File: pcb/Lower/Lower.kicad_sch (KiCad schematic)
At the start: 34 parts

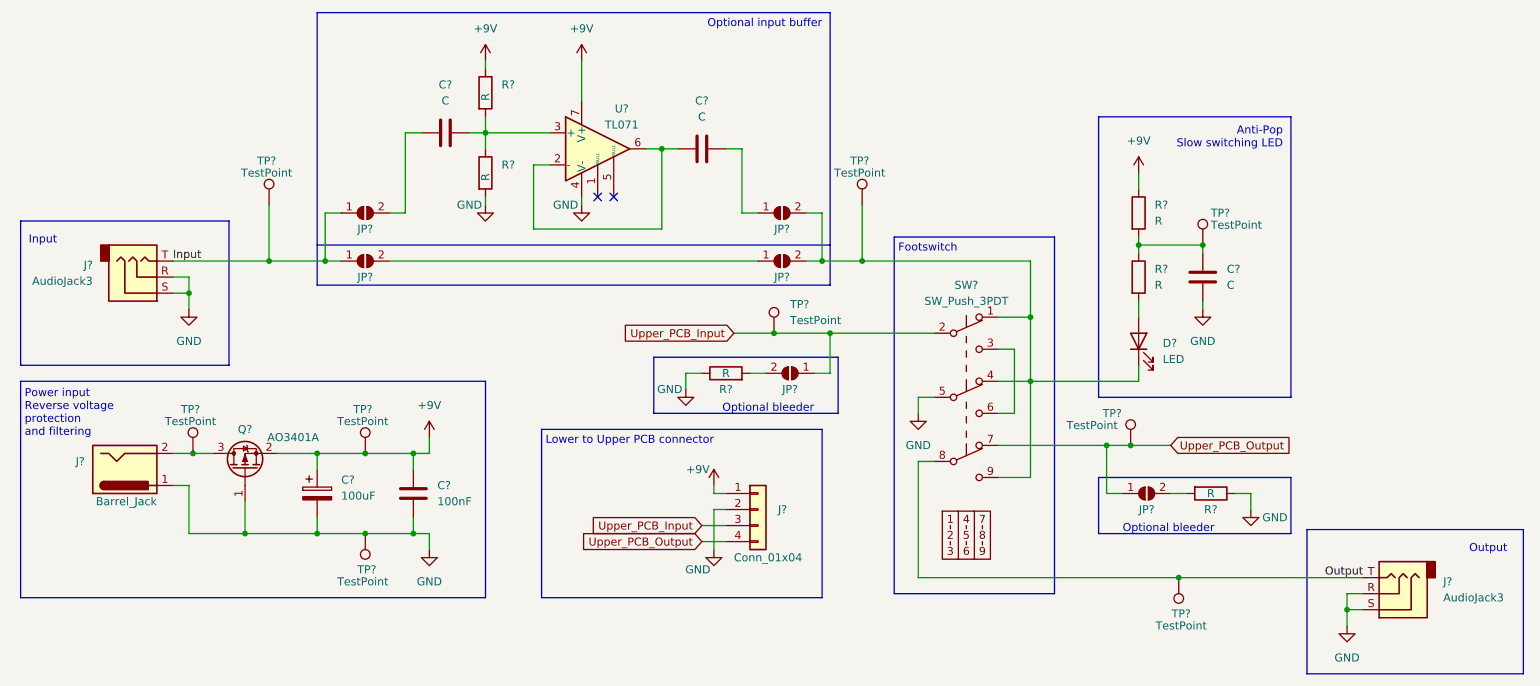
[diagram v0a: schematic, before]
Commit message: Assign Lower PCB footprints and BOM codes
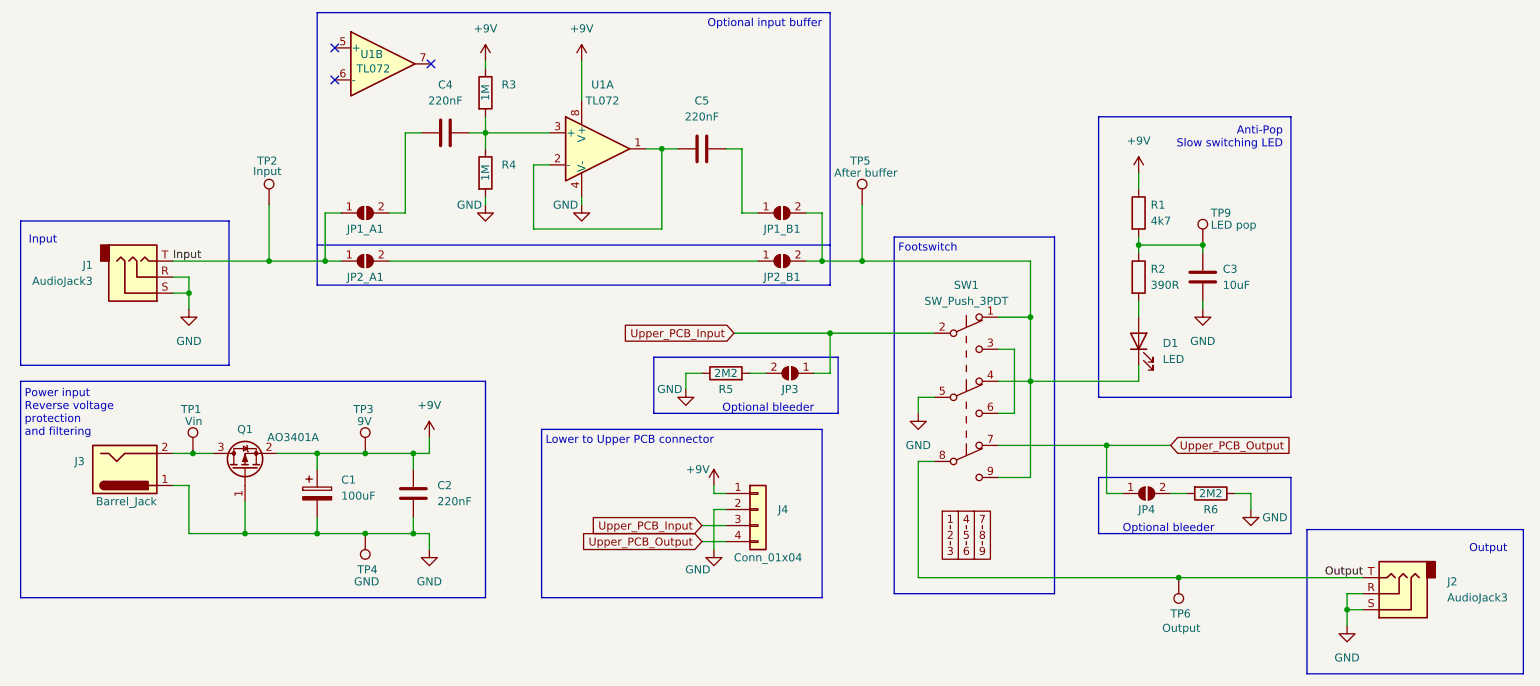
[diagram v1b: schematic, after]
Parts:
- removed C?: 100nF, symbol Device:C
- removed TP? (x2): TestPoint, symbol Connector:TestPoint
- removed U?: TL071, symbol Amplifier_Operational:TL071
- added C2: 220nF, Capacitor_SMD:C_0603_1608Metric, symbol Device:C
- added U1: TL072, Package_SO:SOIC-8_3.9x4.9mm_P1.27mm, symbol Amplifier_Operational:TL072
- C1: renamed from C?; footprint (none) -> Capacitor_SMD:CP_Elec_6.3x5.8; LCSC (none) -> C249982
- C3: renamed from C?; value C -> 10uF; footprint (none) -> Capacitor_SMD:C_0805_2012Metric; LCSC (none) -> C15850
- C4, C5: renamed from C?; value C -> 220nF; footprint (none) -> Capacitor_SMD:C_0603_1608Metric; LCSC (none) -> C21120
- D1: renamed from D?; footprint (none) -> LED_THT:LED_D5.0mm; LCSC (none) -> C417347
- J4: renamed from J?; footprint (none) -> Connector_PinSocket_2.54mm:PinSocket_1x04_P2.54mm_Vertical; now left out of the parts list
- JP1_A1, JP1_B1, JP2_A1, JP2_B1, JP3, JP4: renamed from JP?; footprint (none) -> Jumper:SolderJumper-2_P1.3mm_Open_TrianglePad1.0x1.5mm; now left out of the parts list
- Q1: renamed from Q?; LCSC (none) -> C15127
- R1: renamed from R?; value R -> 4k7; footprint (none) -> Resistor_SMD:R_0603_1608Metric
- R2: renamed from R?; value R -> 390R; footprint (none) -> Resistor_SMD:R_0603_1608Metric
- R3, R4: renamed from R?; value R -> 1M; footprint (none) -> Resistor_SMD:R_0603_1608Metric
- R5, R6: renamed from R?; value R -> 2M2; footprint (none) -> Resistor_SMD:R_0603_1608Metric
- SW1: renamed from SW?; footprint (none) -> MeineBib:Footswitch_3PDT
- TP1: renamed from TP?; value TestPoint -> Vin; footprint (none) -> TestPoint:TestPoint_Pad_D2.0mm; now left out of the parts list
- TP2: renamed from TP?; value TestPoint -> Input; footprint (none) -> TestPoint:TestPoint_Bridge_Pitch2.54mm_Drill1.0mm; now left out of the parts list
- TP3: renamed from TP?; value TestPoint -> 9V; footprint (none) -> TestPoint:TestPoint_Pad_D2.0mm; now left out of the parts list
- TP4: renamed from TP?; value TestPoint -> GND; footprint (none) -> TestPoint:TestPoint_Bridge_Pitch2.54mm_Drill1.0mm; now left out of the parts list
- TP5: renamed from TP?; value TestPoint -> After buffer; footprint (none) -> TestPoint:TestPoint_Pad_D2.0mm; now left out of the parts list
- TP6: renamed from TP?; value TestPoint -> Output; footprint (none) -> TestPoint:TestPoint_Bridge_Pitch2.54mm_Drill1.0mm; now left out of the parts list
- TP9: renamed from TP?; value TestPoint -> LED pop; footprint (none) -> TestPoint:TestPoint_Pad_D2.0mm; now left out of the parts list
- gave numbers to parts that had none: 3
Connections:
- net +9V: now also C2.1, U1.8 (V+)
- net GND: now also C2.2, U1.4 (V-)
- net at C4.2, R3.2, R4.1: now also U1.3 (+)
- net at C5.1: now also U1.1, U1.2 (-)
- no-connect marks 2 -> 3

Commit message: [Lower] Design and add more footprints
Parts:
- J1, J2: footprint (none) -> MeineBib:Audio_Jack_PJ-602B
- J3: footprint (none) -> MeineBib:DC_Barrel_Jack_Thinline_Wired_Standing
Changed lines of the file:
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@@
       (effects (font (size 1.27 1.27)) (justify right))
     )
-    (property "Footprint" "" (id 2) (at 52.07 92.71 0)
+    (property "Footprint" "MeineBib:Audio_Jack_PJ-602B" (id 2) (at 52.07 92.71 0)
       (effects (font (size 1.27 1.27)) hide)
     )
@@
       (effects (font (size 1.27 1.27)) (justify right))
     )
-    (property "Footprint" "" (id 2) (at 50.8 122.174 0)
+    (property "Footprint" "MeineBib:DC_Barrel_Jack_Thinline_Wired_Standing" (id 2) (at 50.8 122.174 0)
       (effects (font (size 1.27 1.27)) hide)
     )
@@
       (effects (font (size 1.27 1.27)) (justify right))
     )
-    (property "Footprint" "" (id 2) (at 250.825 142.875 0)
+    (property "Footprint" "MeineBib:Audio_Jack_PJ-602B" (id 2) (at 250.825 142.875 0)
       (effects (font (size 1.27 1.27)) hide)
     )
@@
     )
     (path "/37778a1f-86de-4449-abb1-14af5009805a"
-      (reference "J1") (unit 1) (value "AudioJack3") (footprint "")
+      (reference "J1") (unit 1) (value "AudioJack3") (footprint "MeineBib:Audio_Jack_PJ-602B")
     )
     (path "/ce833355-b6f2-4a51-9de8-dda19b75db2a"
-      (reference "J2") (unit 1) (value "AudioJack3") (footprint "")
+      (reference "J2") (unit 1) (value "AudioJack3") (footprint "MeineBib:Audio_Jack_PJ-602B")
     )
     (path "/680b3e96-c480-445f-a2bf-28a5c2056d8e"
-      (reference "J3") (unit 1) (value "Barrel_Jack") (footprint "")
+      (reference "J3") (unit 1) (value "Barrel_Jack") (footprint "MeineBib:DC_Barrel_Jack_Thinline_Wired_Standing")
     )
     (path "/43624bd7-5b28-4455-bedf-a59e39f0128d"

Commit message: [Lower] Update Anti-Pop circuit after testing
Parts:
- R2: renamed from R1; value 4k7 -> 2k2
- renumbered R2 to R1
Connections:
- net +9V: now also R1.1; no longer R2.1
- net at D1.2 (A): now also R2.2; no longer R1.2
- net at C3.1, TP9.1: now also R1.2, R2.1; no longer R1.1, R2.2
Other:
- moved on the sheet: R1, R2
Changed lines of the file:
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@@
     (pin "2")
   )
-  (symbol (lib_id "Device:R") (at 210.185 82.55 0) (unit 1)
-    (in_bom yes) (on_board yes) (fields_autoplaced)
-    (property "Reference" "R1" (id 0) (at 212.09 81.2799 0)
-      (effects (font (size 1.27 1.27)) (justify left))
-    )
-    (property "Value" "4k7" (id 1) (at 212.09 83.8199 0)
-      (effects (font (size 1.27 1.27)) (justify left))
-    )
-    (property "Footprint" "Resistor_SMD:R_0603_1608Metric" (id 2) (at 208.407 82.55 90)
-      (effects (font (size 1.27 1.27)) hide)
-    )
-    (property "Datasheet" "~" (id 3) (at 210.185 82.55 0)
+  (symbol (lib_id "Device:R") (at 210.185 92.71 0) (unit 1)
+    (in_bom yes) (on_board yes) (fields_autoplaced)
+    (property "Reference" "R2" (id 0) (at 212.09 91.4399 0)
+      (effects (font (size 1.27 1.27)) (justify left))
+    )
+    (property "Value" "2k2" (id 1) (at 212.09 93.9799 0)
+      (effects (font (size 1.27 1.27)) (justify left))
+    )
+    (property "Footprint" "Resistor_SMD:R_0603_1608Metric" (id 2) (at 208.407 92.71 90)
+      (effects (font (size 1.27 1.27)) hide)
+    )
+    (property "Datasheet" "~" (id 3) (at 210.185 92.71 0)
       (effects (font (size 1.27 1.27)) hide)
     )
@@
     (pin "1")
   )
-  (symbol (lib_id "Device:R") (at 210.185 92.71 0) (unit 1)
-    (in_bom yes) (on_board yes) (fields_autoplaced)
-    (property "Reference" "R2" (id 0) (at 212.09 91.4399 0)
-      (effects (font (size 1.27 1.27)) (justify left))
-    )
-    (property "Value" "390R" (id 1) (at 212.09 93.9799 0)
-      (effects (font (size 1.27 1.27)) (justify left))
-    )
-    (property "Footprint" "Resistor_SMD:R_0603_1608Metric" (id 2) (at 208.407 92.71 90)
-      (effects (font (size 1.27 1.27)) hide)
-    )
-    (property "Datasheet" "~" (id 3) (at 210.185 92.71 0)
+  (symbol (lib_id "Device:R") (at 210.185 82.55 0) (unit 1)
+    (in_bom yes) (on_board yes)
+    (property "Reference" "R1" (id 0) (at 212.09 81.2799 0)
+      (effects (font (size 1.27 1.27)) (justify left))
+    )
+    (property "Value" "390R" (id 1) (at 212.09 83.82 0)
+      (effects (font (size 1.27 1.27)) (justify left))
+    )
+    (property "Footprint" "Resistor_SMD:R_0603_1608Metric" (id 2) (at 208.407 82.55 90)
+      (effects (font (size 1.27 1.27)) hide)
+    )
+    (property "Datasheet" "~" (id 3) (at 210.185 82.55 0)
       (effects (font (size 1.27 1.27)) hide)
     )
@@
       (reference "Q1") (unit 1) (value "AO3401A") (footprint "Package_TO_SOT_SMD:SOT-23")
     )
+    (path "/c5dde4d4-1f05-4ce8-a9a0-135e7142ecd2"
+      (reference "R1") (unit 1) (value "390R") (footprint "Resistor_SMD:R_0603_1608Metric")
+    )
     (path "/0ec435e0-2219-4036-8fc8-9d64c1b535ad"
-      (reference "R1") (unit 1) (value "4k7") (footprint "Resistor_SMD:R_0603_1608Metric")
-    )
-    (path "/c5dde4d4-1f05-4ce8-a9a0-135e7142ecd2"
-      (reference "R2") (unit 1) (value "390R") (footprint "Resistor_SMD:R_0603_1608Metric")
+      (reference "R2") (unit 1) (value "2k2") (footprint "Resistor_SMD:R_0603_1608Metric")
     )
     (path "/6685e374-4b74-4363-b25d-dd27bd2656c7"

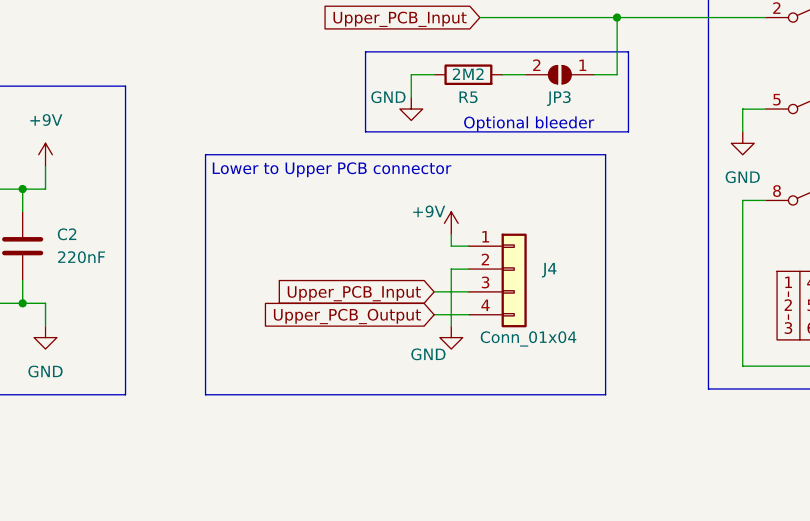
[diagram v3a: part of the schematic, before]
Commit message: [Lower] Pinswap PCB-PCB connector
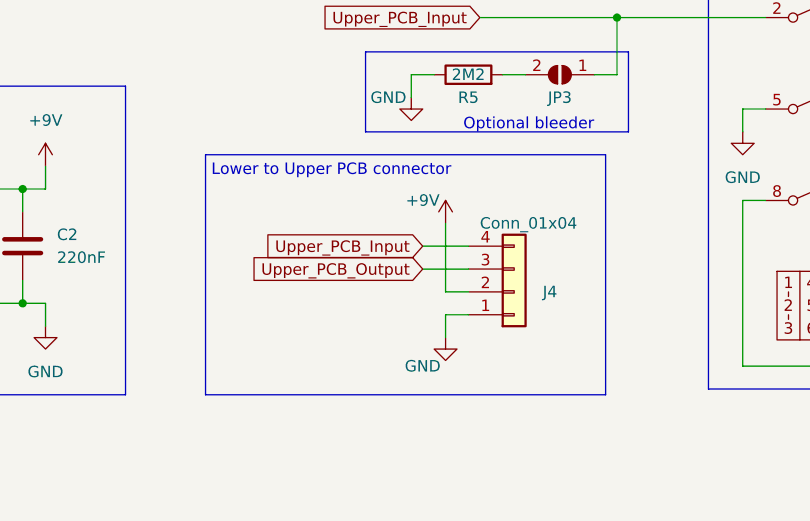
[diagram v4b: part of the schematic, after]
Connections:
- net +9V: now also J4.2 (Pin_2); no longer J4.1 (Pin_1)
- net GND: now also J4.1 (Pin_1); no longer J4.2 (Pin_2)
- net Upper_PCB_Input: now also J4.4 (Pin_4); no longer J4.3 (Pin_3)
- net Upper_PCB_Output: now also J4.3 (Pin_3); no longer J4.4 (Pin_4)
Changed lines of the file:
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@@
+    (stroke (width 0) (type default) (color 0 0 0 0))
+  )
+  (wire (pts (xy 144.78 134.62) (xy 142.24 134.62))
     (stroke (width 0) (type default) (color 0 0 0 0))
   )
@@
     (stroke (width 0) (type default) (color 0 0 0 0))
   )
+  (wire (pts (xy 142.24 124.46) (xy 142.24 132.08))
+    (stroke (width 0) (type default) (color 0 0 0 0))
+  )
   (wire (pts (xy 104.14 69.85) (xy 106.68 69.85))
     (stroke (width 0) (type default) (color 0 0 0 0))
@@
     (stroke (width 0) (type default) (color 0 0 0 0))
   )
-  (wire (pts (xy 140.97 134.62) (xy 144.78 134.62))
-    (stroke (width 0) (type default) (color 0 0 0 0))
-  )
   (polyline (pts (xy 66.04 106.68) (xy 66.04 83.82))
     (stroke (width 0) (type default) (color 0 0 0 0))
@@
     (stroke (width 0) (type default) (color 0 0 0 0))
   )
-  (wire (pts (xy 144.78 129.54) (xy 142.875 129.54))
-    (stroke (width 0) (type default) (color 0 0 0 0))
-  )
   (wire (pts (xy 80.01 130.81) (xy 80.01 133.35))
     (stroke (width 0) (type default) (color 0 0 0 0))
@@
     (stroke (width 0) (type default) (color 0 0 0 0))
   )
-  (wire (pts (xy 140.97 132.08) (xy 144.78 132.08))
-    (stroke (width 0) (type default) (color 0 0 0 0))
-  )
   (polyline (pts (xy 33.02 109.22) (xy 106.68 109.22))
     (stroke (width 0) (type default) (color 0 0 0 0))
@@
     (stroke (width 0) (type default) (color 0 0 0 0))
   )
+  (wire (pts (xy 139.7 129.54) (xy 144.78 129.54))
+    (stroke (width 0) (type default) (color 0 0 0 0))
+  )
   (wire (pts (xy 158.75 107.95) (xy 161.29 107.95))
     (stroke (width 0) (type default) (color 0 0 0 0))
@@
     (stroke (width 0) (type default) (color 0 0 0 0))
   )
+  (wire (pts (xy 142.24 134.62) (xy 142.24 137.16))
+    (stroke (width 0) (type default) (color 0 0 0 0))
+  )
   (polyline (pts (xy 171.45 86.36) (xy 196.85 86.36))
     (stroke (width 0) (type default) (color 0 0 0 0))
@@
     (stroke (width 0) (type default) (color 0 0 0 0))
   )
-  (wire (pts (xy 144.78 127) (xy 142.875 127))
-    (stroke (width 0) (type default) (color 0 0 0 0))
-  )
   (polyline (pts (xy 203.835 124.46) (xy 203.835 133.35))
     (stroke (width 0) (type default) (color 0 0 0 0))
@@
     (stroke (width 0) (type default) (color 0 0 0 0))
   )
+  (wire (pts (xy 139.7 127) (xy 144.78 127))
+    (stroke (width 0) (type default) (color 0 0 0 0))
+  )
   (wire (pts (xy 93.98 82.55) (xy 93.98 69.85))
     (stroke (width 0) (type default) (color 0 0 0 0))
@@
     (stroke (width 0) (type default) (color 0 0 0 0))
   )
-  (wire (pts (xy 142.875 129.54) (xy 142.875 135.89))
-    (stroke (width 0) (type default) (color 0 0 0 0))
-  )
   (wire (pts (xy 68.58 128.27) (xy 68.58 133.35))
     (stroke (width 0) (type default) (color 0 0 0 0))
@@
     (stroke (width 0) (type default) (color 0 0 0 0))
   )
+  (wire (pts (xy 142.24 132.08) (xy 144.78 132.08))
+    (stroke (width 0) (type default) (color 0 0 0 0))
+  )
   (polyline (pts (xy 106.68 109.22) (xy 106.68 143.51))
     (stroke (width 0) (type default) (color 0 0 0 0))
@@
   )
   (polyline (pts (xy 203.835 111.76) (xy 234.315 111.76))
-    (stroke (width 0) (type default) (color 0 0 0 0))
-  )
-  (wire (pts (xy 142.875 127) (xy 142.875 125.73))
     (stroke (width 0) (type default) (color 0 0 0 0))
   )
@@
     (effects (font (size 1.27 1.27)) (justify right bottom))
   )
-  (global_label "Upper_PCB_Input" (shape input) (at 140.97 132.08 180) (fields_autoplaced)
+  (global_label "Upper_PCB_Input" (shape input) (at 139.7 127 180) (fields_autoplaced)
     (effects (font (size 1.27 1.27)) (justify right))
-    (property "Intersheet References" "${INTERSHEET_REFS}" (id 0) (at 122.5307 132.0006 0)
+    (property "Intersheet References" "${INTERSHEET_REFS}" (id 0) (at 121.2607 126.9206 0)
       (effects (font (size 1.27 1.27)) (justify right) hide)
     )
@@
     )
   )
-  (global_label "Upper_PCB_Output" (shape input) (at 140.97 134.62 180) (fields_autoplaced)
+  (global_label "Upper_PCB_Output" (shape input) (at 139.7 129.54 180) (fields_autoplaced)
     (effects (font (size 1.27 1.27)) (justify right))
-    (property "Intersheet References" "${INTERSHEET_REFS}" (id 0) (at 121.0793 134.6994 0)
+    (property "Intersheet References" "${INTERSHEET_REFS}" (id 0) (at 119.8093 129.6194 0)
       (effects (font (size 1.27 1.27)) (justify right) hide)
     )
@@
     (pin "1")
   )
-  (symbol (lib_id "Connector_Generic:Conn_01x04") (at 149.86 129.54 0) (unit 1)
-    (in_bom no) (on_board yes)
-    (property "Reference" "J4" (id 0) (at 153.035 129.5399 0)
-      (effects (font (size 1.27 1.27)) (justify left))
-    )
-    (property "Value" "Conn_01x04" (id 1) (at 146.05 137.16 0)
-      (effects (font (size 1.27 1.27)) (justify left))
-    )
-    (property "Footprint" "Connector_PinSocket_2.54mm:PinSocket_1x04_P2.54mm_Vertical" (id 2) (at 149.86 129.54 0)
-      (effects (font (size 1.27 1.27)) hide)
-    )
-    (property "Datasheet" "~" (id 3) (at 149.86 129.54 0)
+  (symbol (lib_id "Connector_Generic:Conn_01x04") (at 149.86 132.08 0) (mirror x) (unit 1)
+    (in_bom no) (on_board yes)
+    (property "Reference" "J4" (id 0) (at 153.035 132.0801 0)
+      (effects (font (size 1.27 1.27)) (justify left))
+    )
+    (property "Value" "Conn_01x04" (id 1) (at 146.05 124.46 0)
+      (effects (font (size 1.27 1.27)) (justify left))
+    )
+    (property "Footprint" "Connector_PinSocket_2.54mm:PinSocket_1x04_P2.54mm_Vertical" (id 2) (at 149.86 132.08 0)
+      (effects (font (size 1.27 1.27)) hide)
+    )
+    (property "Datasheet" "~" (id 3) (at 149.86 132.08 0)
       (effects (font (size 1.27 1.27)) hide)
     )
@@
     (pin "2")
   )
-  (symbol (lib_id "power:GND") (at 142.875 135.89 0) (unit 1)
-    (in_bom yes) (on_board yes)
-    (property "Reference" "#PWR010" (id 0) (at 142.875 142.24 0)
-      (effects (font (size 1.27 1.27)) hide)
-    )
-    (property "Value" "GND" (id 1) (at 140.335 139.065 0))
-    (property "Footprint" "" (id 2) (at 142.875 135.89 0)
-      (effects (font (size 1.27 1.27)) hide)
-    )
-    (property "Datasheet" "" (id 3) (at 142.875 135.89 0)
+  (symbol (lib_id "power:GND") (at 142.24 137.16 0) (unit 1)
+    (in_bom yes) (on_board yes)
+    (property "Reference" "#PWR010" (id 0) (at 142.24 143.51 0)
+      (effects (font (size 1.27 1.27)) hide)
+    )
+    (property "Value" "GND" (id 1) (at 139.7 140.335 0))
+    (property "Footprint" "" (id 2) (at 142.24 137.16 0)
+      (effects (font (size 1.27 1.27)) hide)
+    )
+    (property "Datasheet" "" (id 3) (at 142.24 137.16 0)
       (effects (font (size 1.27 1.27)) hide)
     )
@@
     (pin "1")
   )
-  (symbol (lib_id "power:+9V") (at 142.875 125.73 0) (unit 1)
-    (in_bom yes) (on_board yes)
-    (property "Reference" "#PWR09" (id 0) (at 142.875 129.54 0)
-      (effects (font (size 1.27 1.27)) hide)
-    )
-    (property "Value" "+9V" (id 1) (at 140.335 123.19 0))
-    (property "Footprint" "" (id 2) (at 142.875 125.73 0)
-      (effects (font (size 1.27 1.27)) hide)
-    )
-    (property "Datasheet" "" (id 3) (at 142.875 125.73 0)
-      (effects (font (size 1.27 1.27)) hide)
-    )
+  (symbol (lib_id "power:+9V") (at 142.24 124.46 0) (unit 1)
+    (in_bom yes) (on_board yes)
+    (property "Reference" "#PWR09" (id 0) (at 142.24 128.27 0)
+      (effects (font (size 1.27 1.27)) hide)
+    )
+    (property "Value" "+9V" (id 1) (at 139.7 121.92 0))
+    (property "Footprint" "" (id 2) (at 142.24 124.46 0)
+      (effects (font (size 1.27 1.27)) hide)
+    )
+    (property "Datasheet" "" (id 3) (at 142.24 124.46 0)
+      (effects (font (size 1.27 1.27)) hide)
+    )

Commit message: [Lower] Swap out C1 footprint / LCSC part for THT one
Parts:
- C1: footprint Capacitor_SMD:CP_Elec_6.3x5.8 -> Capacitor_THT:CP_Radial_D5.0mm_P2.00mm; LCSC C249982 -> C108360
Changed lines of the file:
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@@
       (effects (font (size 1.27 1.27)) (justify left))
     )
-    (property "Footprint" "Capacitor_SMD:CP_Elec_6.3x5.8" (id 2) (at 80.9752 130.81 0)
+    (property "Footprint" "Capacitor_THT:CP_Radial_D5.0mm_P2.00mm" (id 2) (at 80.9752 130.81 0)
       (effects (font (size 1.27 1.27)) hide)
     )
@@
       (effects (font (size 1.27 1.27)) hide)
     )
-    (property "LCSC" "C249982" (id 4) (at 80.01 127 0)
+    (property "LCSC" "C108360" (id 4) (at 80.01 127 0)
       (effects (font (size 1.27 1.27)) hide)
     )
@@
     )
     (path "/31e113a3-75ac-4b67-b24f-232c1de5df02"
-      (reference "C1") (unit 1) (value "100uF") (footprint "Capacitor_SMD:CP_Elec_6.3x5.8")
+      (reference "C1") (unit 1) (value "100uF") (footprint "Capacitor_THT:CP_Radial_D5.0mm_P2.00mm")
     )
     (path "/805bb281-1ea5-4d98-aae7-592aceb50ea3"
